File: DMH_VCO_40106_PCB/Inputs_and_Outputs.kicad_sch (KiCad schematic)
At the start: 18 parts, among them J1 TS_Jack_6.35mm_Sw, J150 Conn_01x12, J2 TS_Jack_6.35mm_Sw, J200 IDC_02x05, J3 TS_Jack_6.35mm_Sw, J4 TS_Jack_6.35mm_Sw, J5 TS_Jack_6.35mm_Sw, J6 TS_Jack_6.35mm_Sw, J7 TS_Jack_6.35mm_Sw, J8 TS_Jack_6.35mm_Sw, J9 TS_Jack_6.35mm_Sw, SW1 SW_SPDT_321_OnOff, SW2 SW_SPDT_321_OnOff

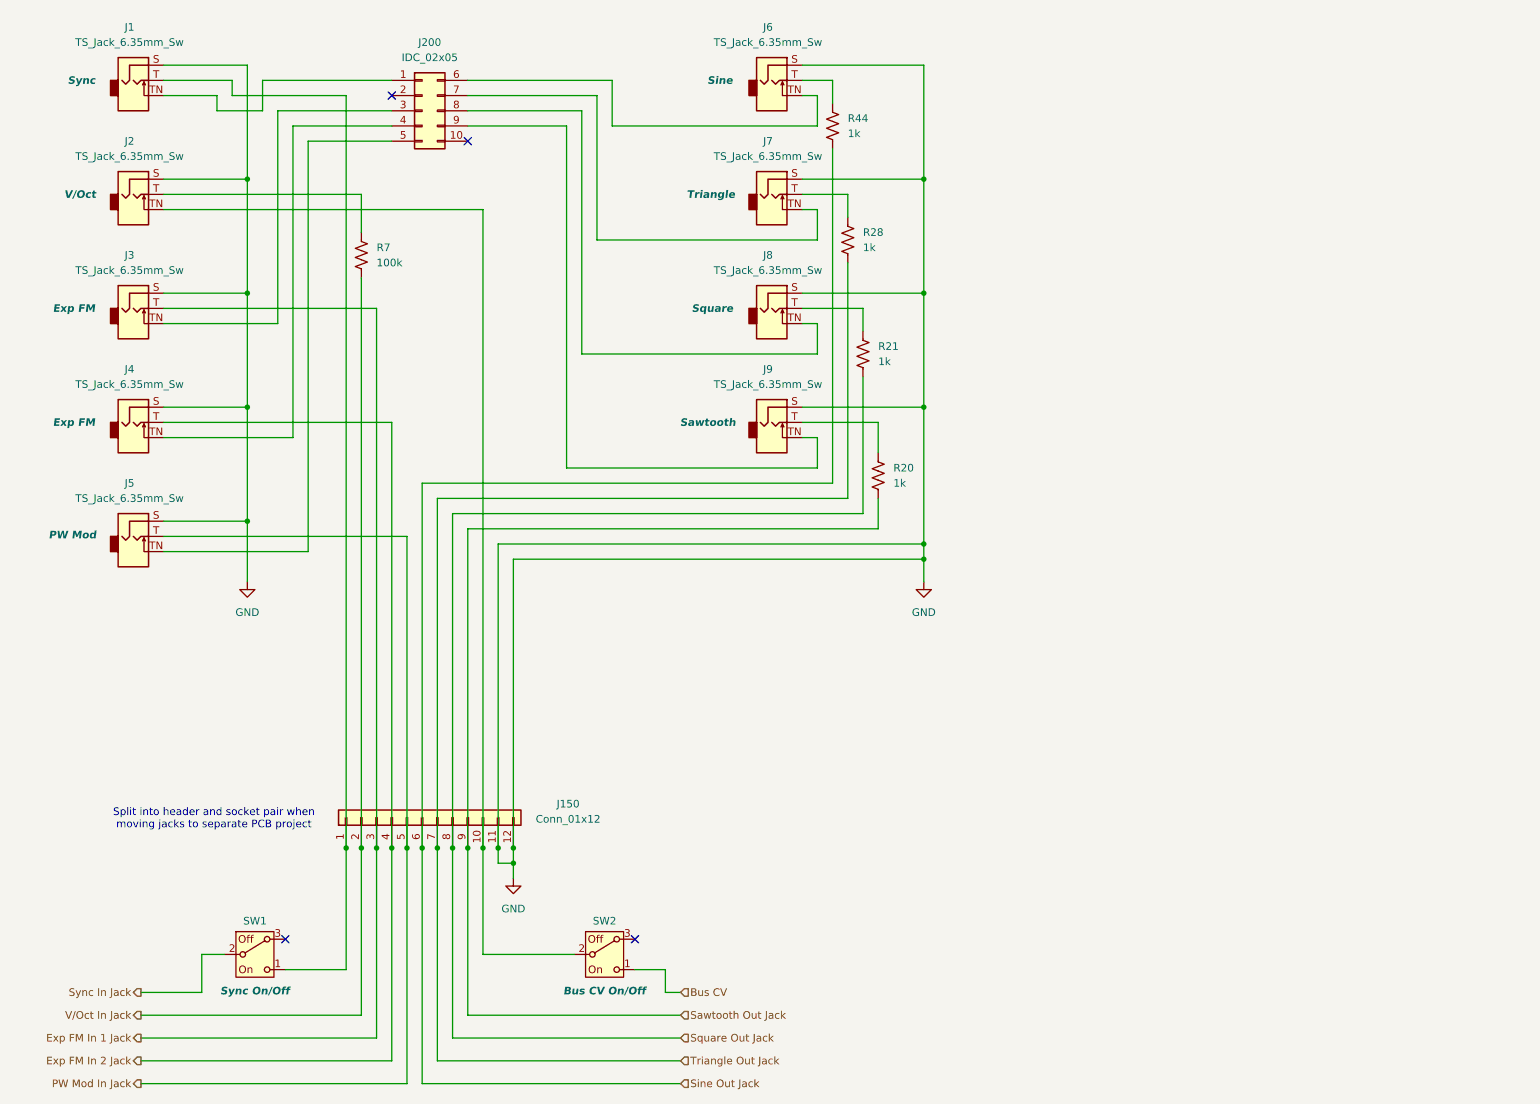
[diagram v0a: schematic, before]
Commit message: Added pcb project separation note
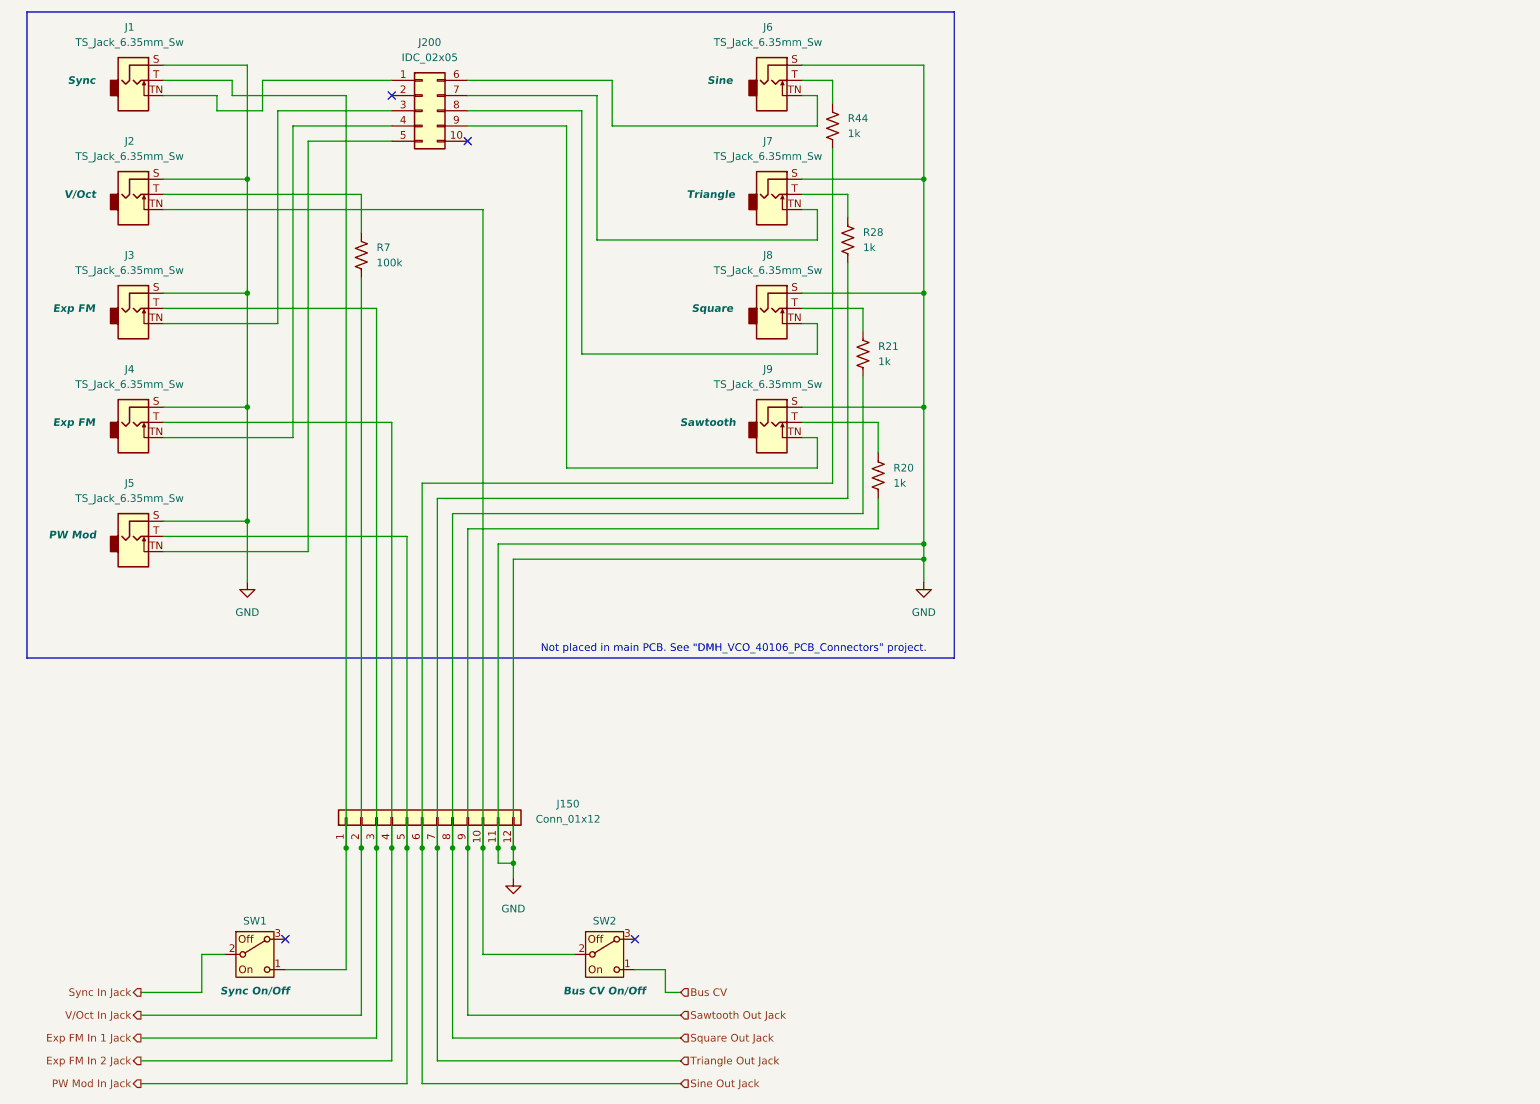
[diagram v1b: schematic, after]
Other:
- note added: "Not placed in main PCB. See "DMH_VCO_40106_PCB_Connectors" project."
- note removed: "Split into header and socket pair when moving jacks to separate PCB project"
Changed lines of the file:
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@@
 		)
 	)
-	(text "Split into header and socket pair when\nmoving jacks to separate PCB project"
+	(rectangle
+		(start 46.99 13.97)
+		(end 201.93 121.92)
+		(stroke
+			(width 0)
+			(type default)
+		)
+		(fill
+			(type none)
+		)
+	)
+	(text "Not placed in main PCB. See \"DMH_VCO_40106_PCB_Connectors\" project."
 		(exclude_from_sim no)
-		(at 78.232 148.844 0)
+		(at 165.1 120.396 0)
 		(effects
 			(font

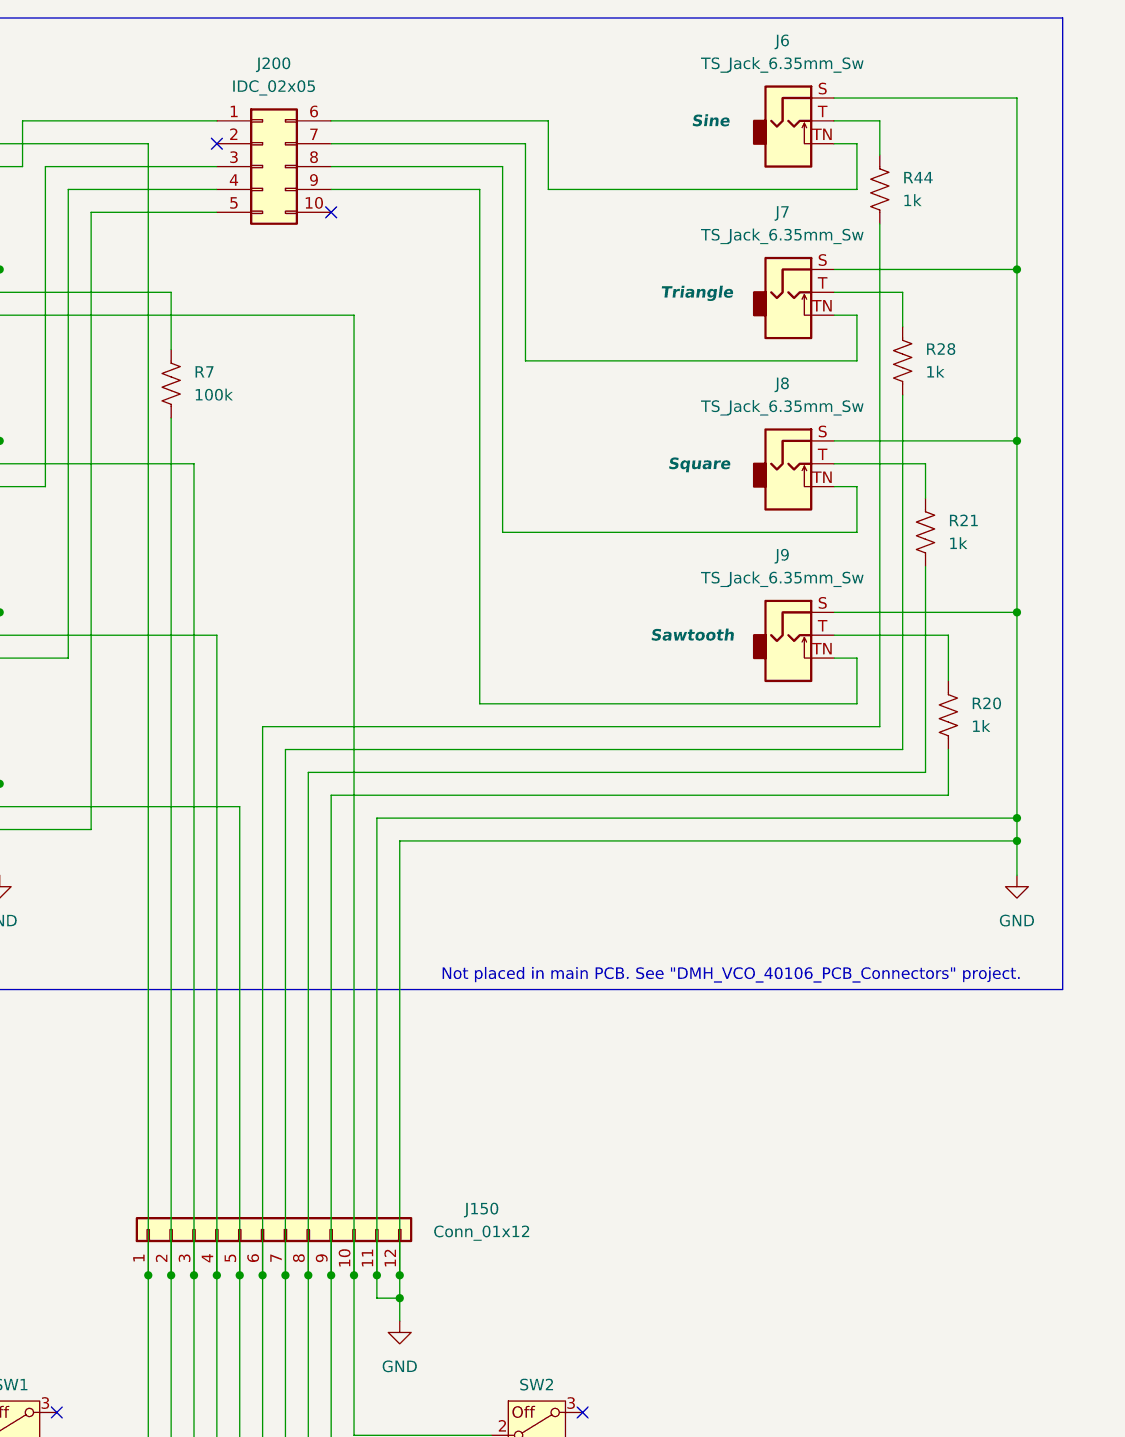
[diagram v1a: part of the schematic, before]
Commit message: Placed input and output resistors back in main PCB
This ensures a more clear schematic and leaves the Connectors PCB only with actual connectors.
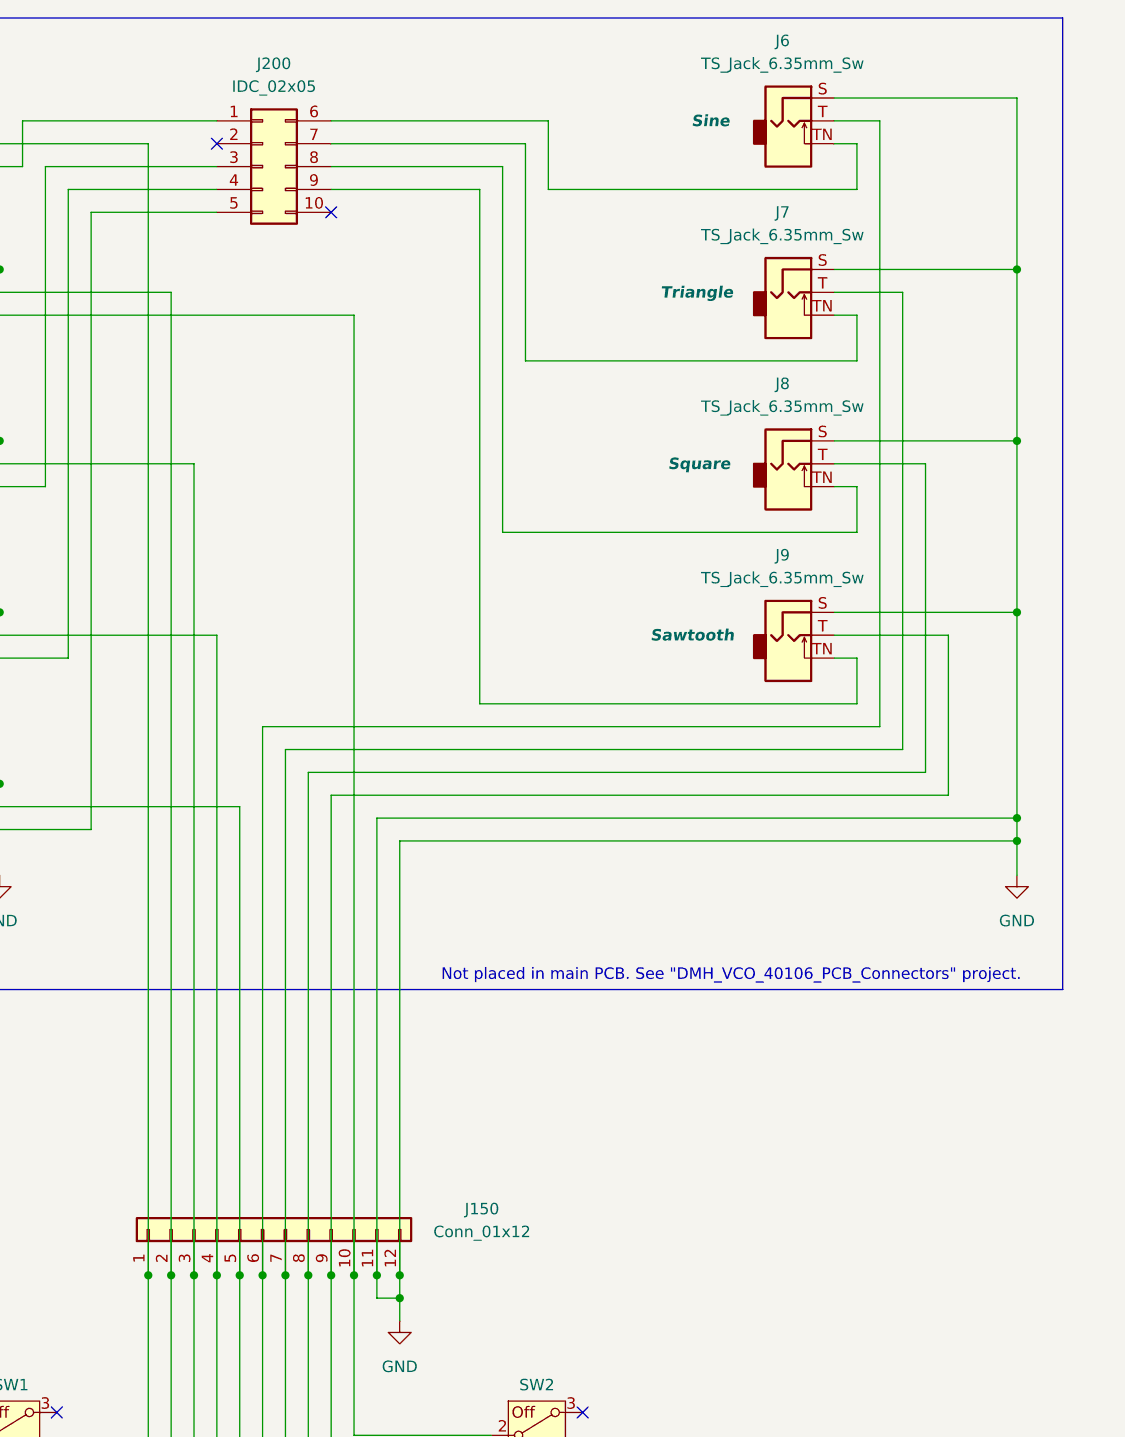
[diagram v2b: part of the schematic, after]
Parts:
- removed R20, R21, R28, R44: 1k, Resistor_THT:R_Axial_DIN0207_L6.3mm_D2.5mm_P7.62mm_Horizontal, symbol Device:R_US
- removed R7: 100k, Resistor_THT:R_Axial_DIN0207_L6.3mm_D2.5mm_P7.62mm_Horizontal, symbol Device:R_US
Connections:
- net Sawtooth Out Jack: now also J9.T
- net Sine Out Jack: now also J6.T
- net Square Out Jack: now also J8.T
- net Triangle Out Jack: now also J7.T
- net V/Oct In Jack: now also J2.T

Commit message: Prepared PCBs for fabrication
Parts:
- J3, J4: Function Exp FM -> Exp FM 2
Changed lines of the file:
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@@
 			)
 		)
-		(property "Function" "Exp FM"
+		(property "Function" "Exp FM 2"
 			(at 54.864 63.5 0)
 			(effects
@@
 			)
 		)
-		(property "Function" "Exp FM"
+		(property "Function" "Exp FM 2"
 			(at 54.864 82.55 0)
 			(effects
